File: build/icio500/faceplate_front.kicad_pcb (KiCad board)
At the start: 4 copper layers, 38.1 x 133.3 mm, 3 parts

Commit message: Restore finished 10-27 faceplate & satellite; maintain summer VPR card edge with zero DRC violations
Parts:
- moved MH1 2.39 mm to (19.1, 6.35)
- moved MH2 2.39 mm to (19.1, 127.0)
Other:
- outline, holes or cut-outs redrawn
- board text added: "+4"
- board text added: "-12"
- board text added: "-16"
- board text added: "-24"
- board text added: "-30"
- board text added: "-4"
- board text added: "-8"
- board text added: "CLIP"
- board text added: "GAIN"
- board text added: "ICIO 500"
- board text added: "LEVEL"
- board text added: "WISPY AUDIO"
- board text added: "dBu"

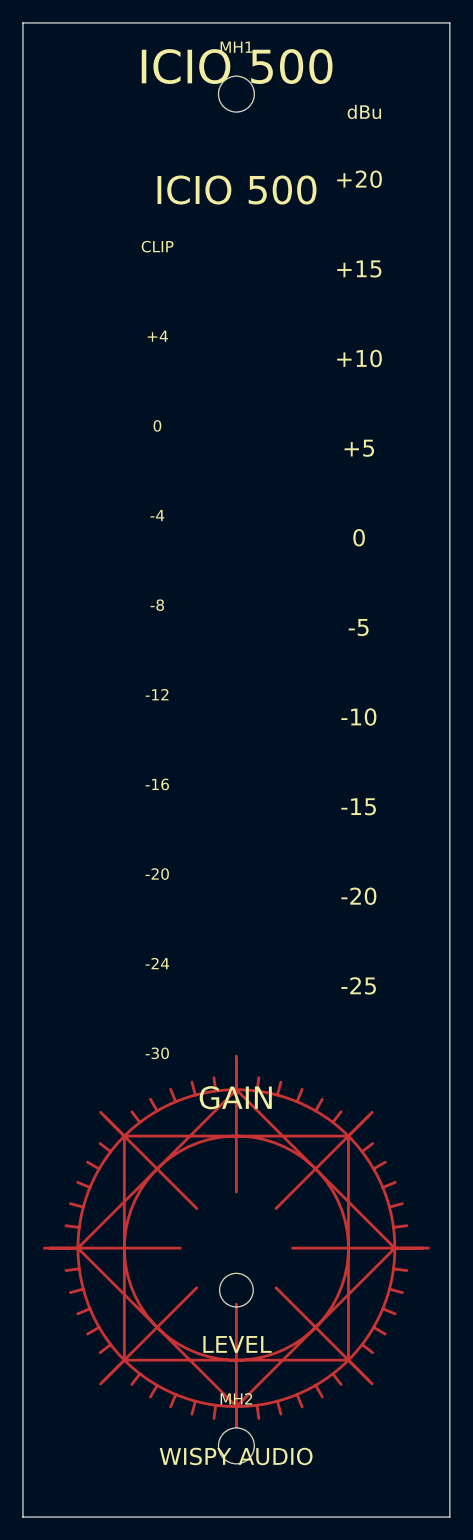
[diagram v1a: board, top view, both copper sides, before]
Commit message: Restore VPR summer board outline (Y=160mm, 26mm bottom notch), align lower bracket BR2, purge vestigial files
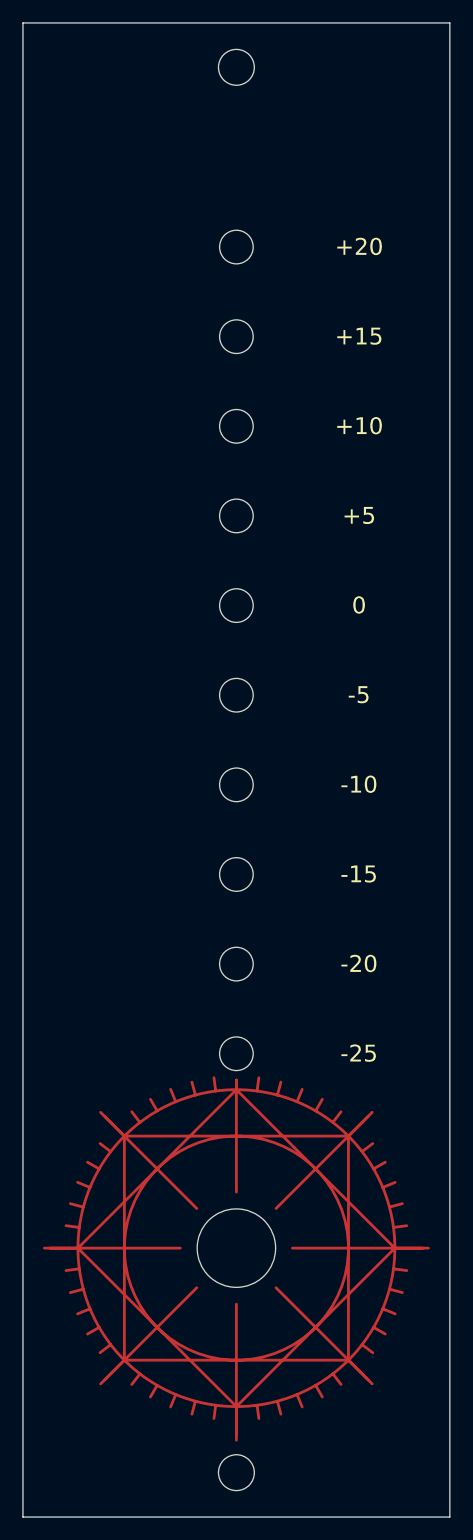
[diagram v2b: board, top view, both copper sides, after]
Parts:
- moved MH1 2.39 mm to (19.1, 3.96)
- moved MH2 2.39 mm to (19.1, 129.4)
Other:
- outline, holes or cut-outs redrawn
- board text removed: "+4"
- board text removed: "-12"
- board text removed: "-16"
- board text removed: "-24"
- board text removed: "-30"
- board text removed: "-4"
- board text removed: "-8"
- board text removed: "CLIP"
- board text removed: "GAIN"
- board text removed: "ICIO 500"
- board text removed: "LEVEL"
- board text removed: "WISPY AUDIO"
- board text removed: "dBu"
